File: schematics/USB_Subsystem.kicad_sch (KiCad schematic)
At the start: 0 parts

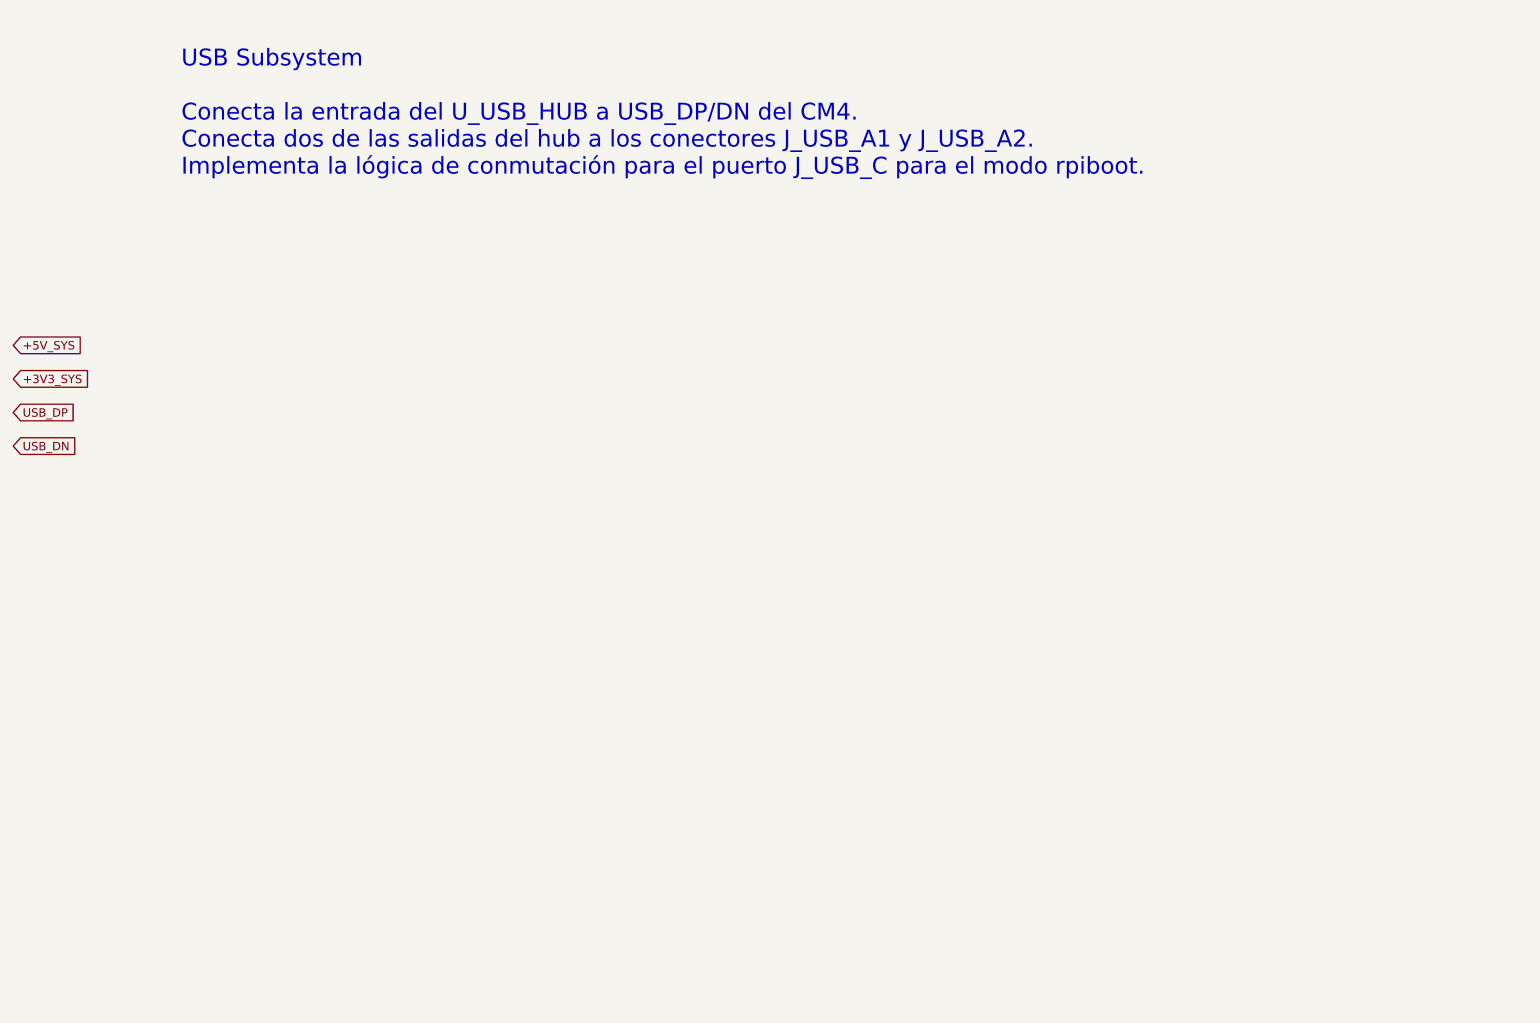
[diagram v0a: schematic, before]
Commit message: Añadir esquemático detallado del subsistema USB
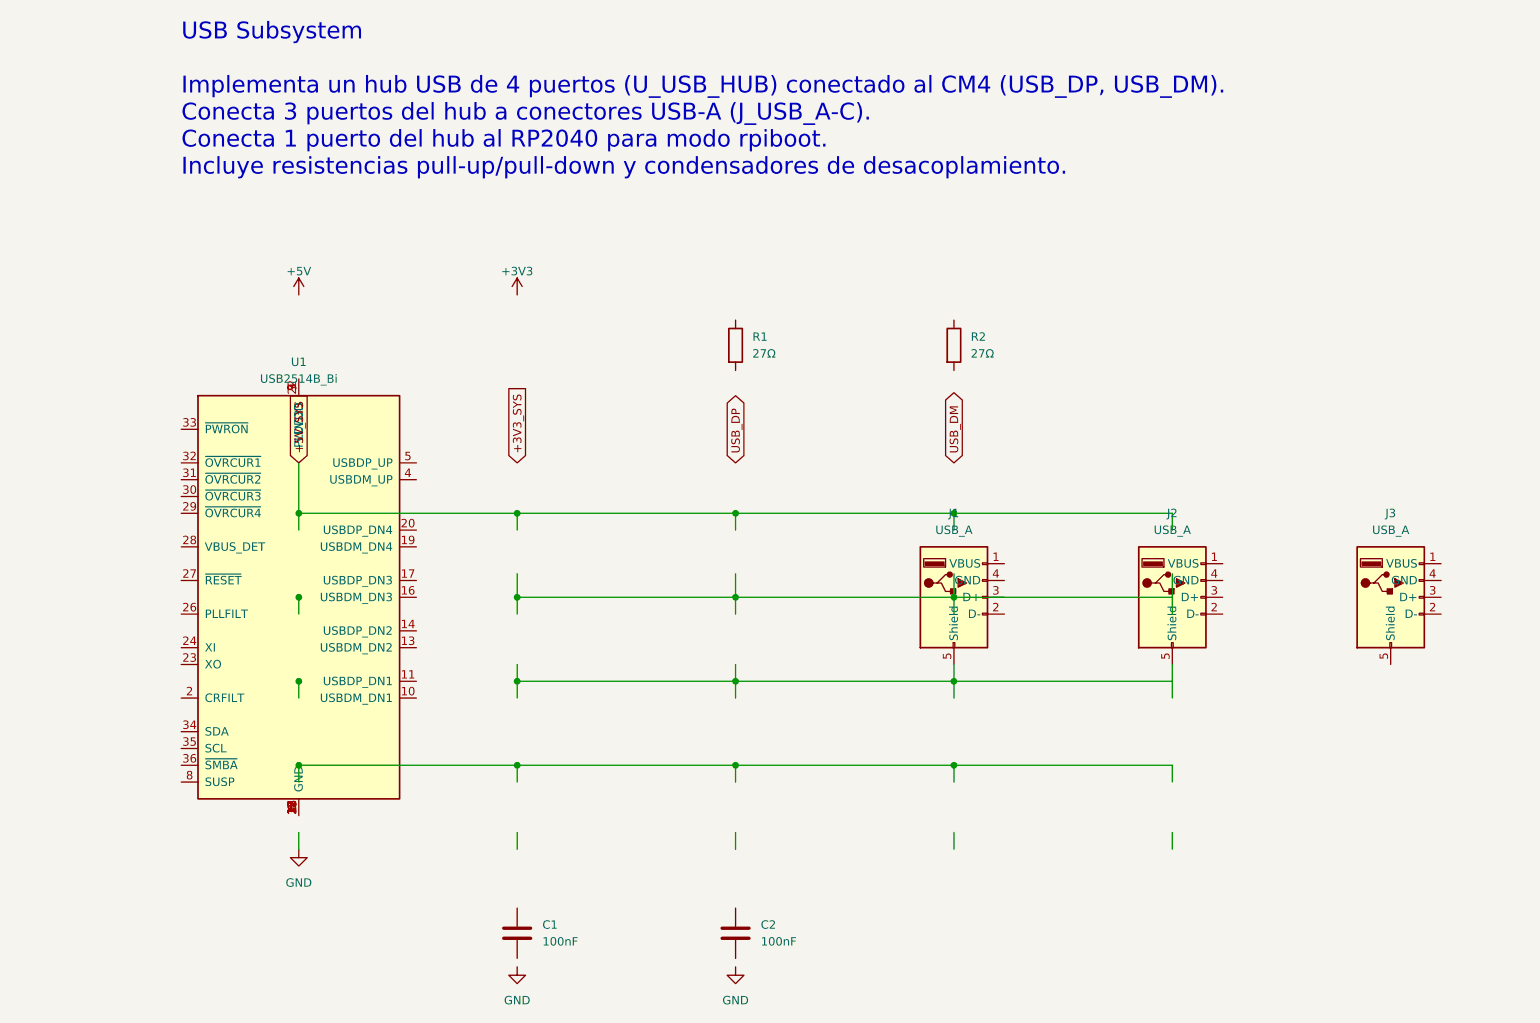
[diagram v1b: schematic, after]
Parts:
- added C1, C2: 100nF, Capacitor_SMD:C_0402_1005Metric, symbol Device:C
- added J1, J2, J3: USB_A, Connector_USB:USB_A_CNCTech_1001-011-01101_Horizontal, symbol Connector:USB_A
- added R1, R2: 27Ω, Resistor_SMD:R_0402_1005Metric, symbol Device:R
- added U1: USB2514B_Bi, Package_DFN_QFN:QFN-36-1EP_6x6mm_P0.5mm_EP3.7x3.7mm, symbol Interface_USB:USB2514B_Bi
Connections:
- new net: U1.1 (GND), U1.12 (GND), U1.15 (GND), U1.18 (GND), U1.21 (GND), U1.25 (GND), U1.37 (GND), U1.6 (GND)
- new net: U1.22 (PLLVDD), U1.3 (VDD33), U1.7 (VDD33), U1.9 (VDD33)
- new net: J1.5 (Shield), J2.5 (Shield)
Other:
- note added: "USB Subsystem Implementa un hub USB de 4 puertos (U_USB_HUB) conectado al CM4 (USB_DP, USB_DM). Conecta 3 puertos del hub a conectores USB-A (J_USB_A-C). Conecta 1 puerto del hub al RP2040 para modo rpiboot. Incluye resistencias pull-up/pull-down y condensadores de desacoplamiento."
- note removed: "USB Subsystem Conecta la entrada del U_USB_HUB a USB_DP/DN del CM4. Conecta dos de las salidas del hub a los conectores J_USB_A1 y J_USB_A2. Implementa la lógica de conmutación para el puerto J_USB_C para el modo rpiboot."
